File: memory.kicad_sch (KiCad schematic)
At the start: 43 parts, among them U1001 AM6231ASGGGAALW, U5001 K4AAG165WA-BCWE

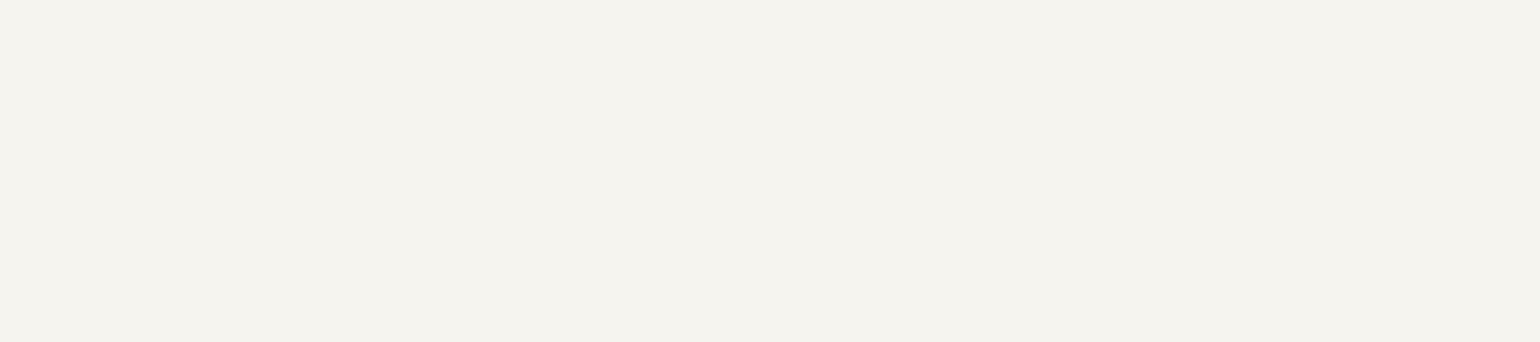
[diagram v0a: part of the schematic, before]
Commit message: Cleaned up schematic
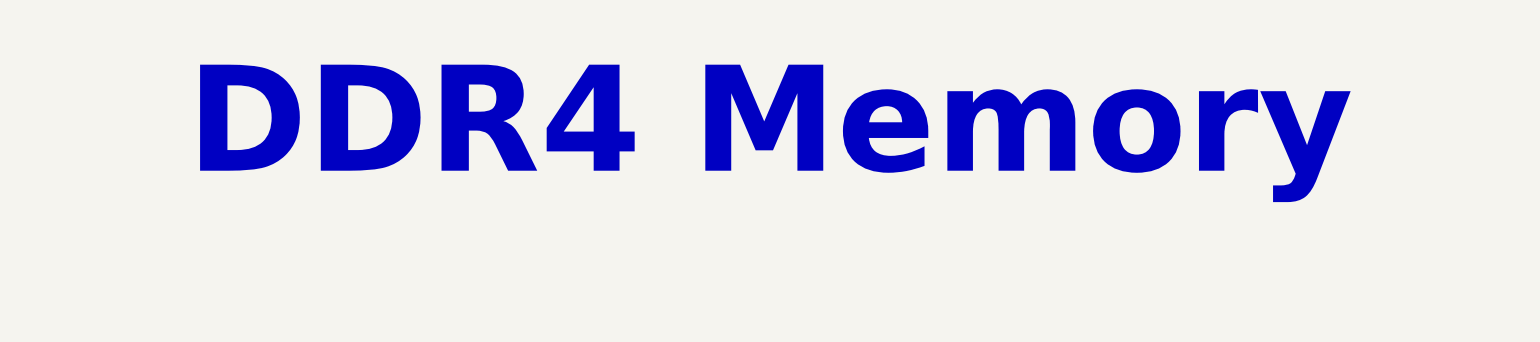
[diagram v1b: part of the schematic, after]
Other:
- note added: "DDR4 Memory"
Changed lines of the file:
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@@
+		)
+	)
+	(text "DDR4 Memory"
+		(exclude_from_sim no)
+		(at 187.452 47.498 0)
+		(effects
+			(font
+				(size 17.78 17.78)
+				(thickness 3.556)
+				(bold yes)
+			)
 		)
 	)

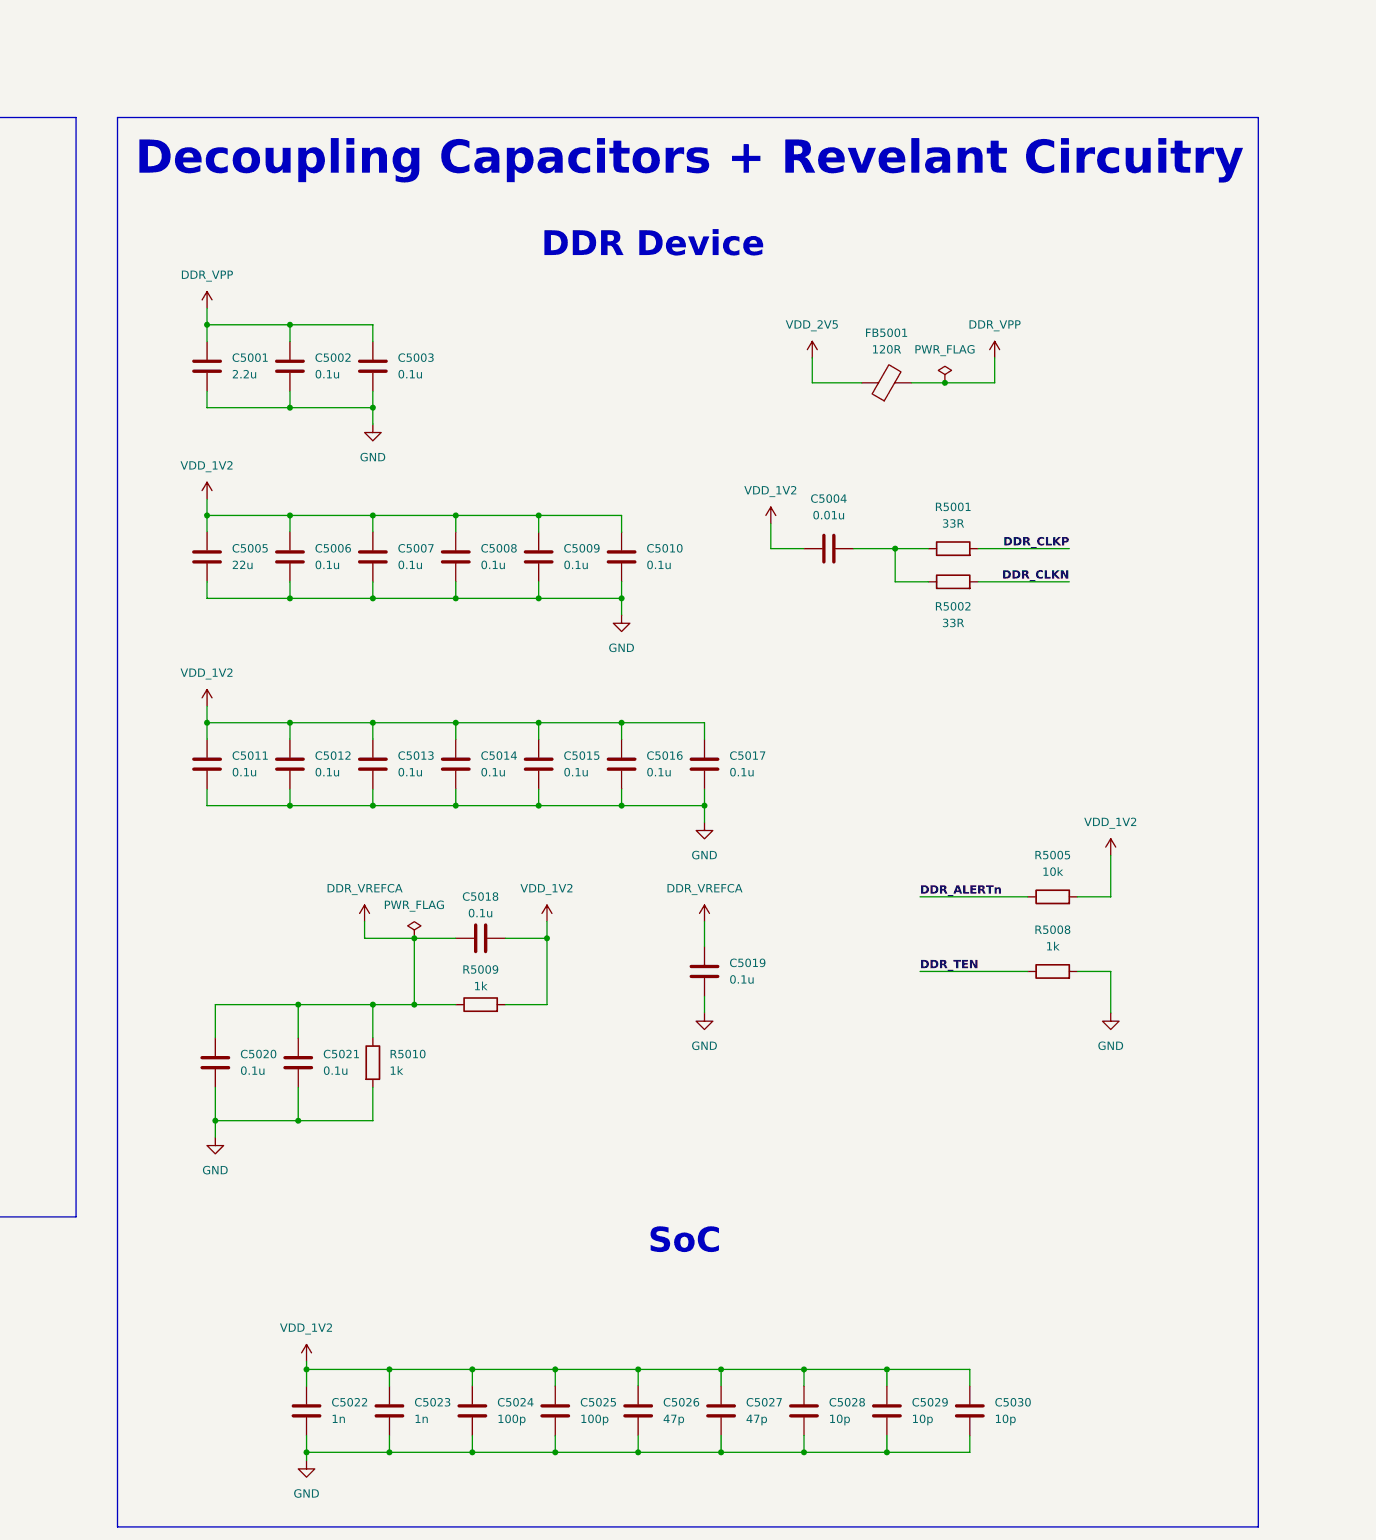
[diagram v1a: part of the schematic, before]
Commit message: Changed DDR4 decoupling capacitors and placed them
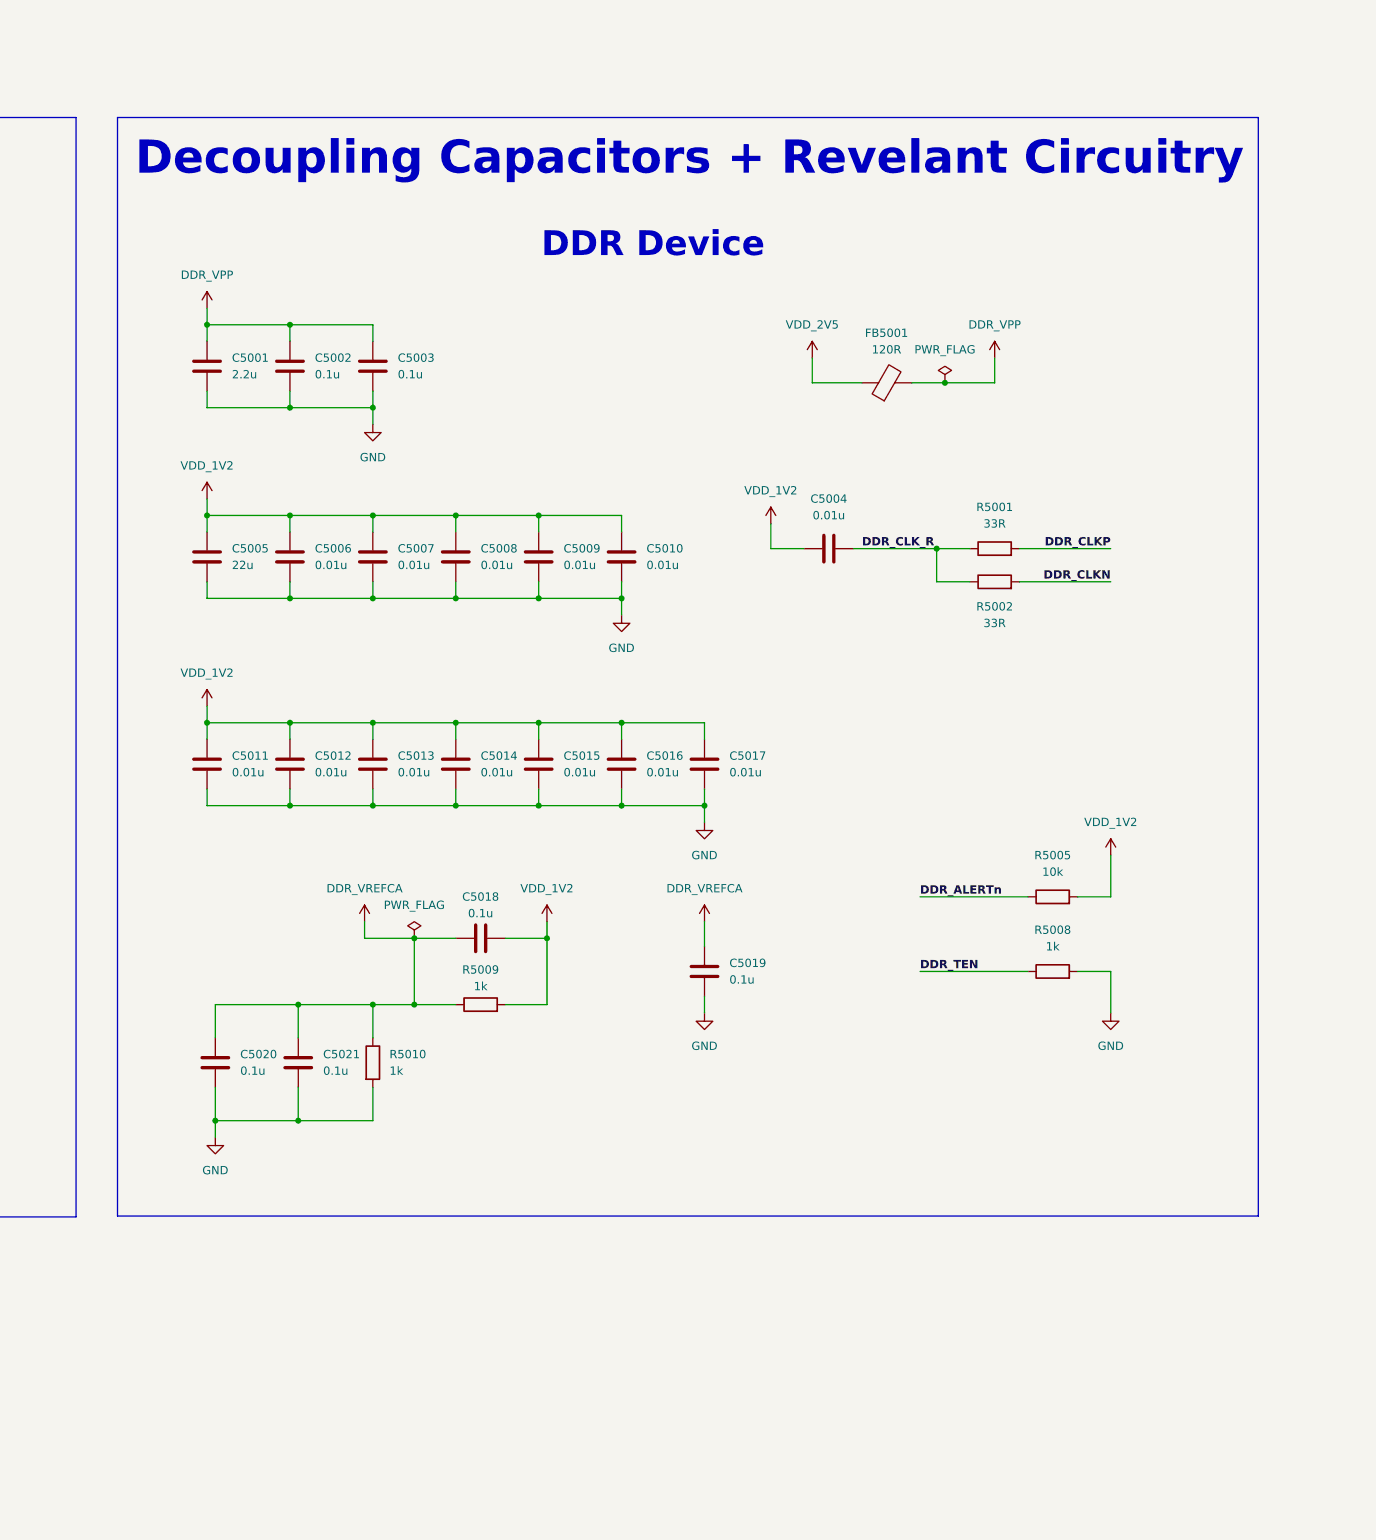
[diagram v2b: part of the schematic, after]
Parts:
- removed C5022, C5023: 1n, Capacitor_SMD:C_0201_0603Metric, symbol Device:C
- removed C5024, C5025: 100p, Capacitor_SMD:C_0201_0603Metric, symbol Device:C
- removed C5026, C5027: 47p, Capacitor_SMD:C_0201_0603Metric, symbol Device:C
- removed C5028, C5029, C5030: 10p, Capacitor_SMD:C_0201_0603Metric, symbol Device:C
- C5006, C5007, C5008, C5009, C5010, C5011, C5012, C5013, C5014, C5015, C5016, C5017: value 0.1u -> 0.01u
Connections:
- net DDR_CLK_R: now reaches C5004.2, R5001.1, R5002.1
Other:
- note removed: "SoC"
- moved on the sheet: R5001, R5002

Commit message: Placed all DDR4 external circuitry and added power puddles
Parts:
- R5005, R5008, R5009, R5010: footprint Resistor_SMD:R_0402_1005Metric -> Resistor_SMD:R_0201_0603Metric
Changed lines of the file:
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@@
 			)
 		)
-		(property "Footprint" "Resistor_SMD:R_0402_1005Metric"
+		(property "Footprint" "Resistor_SMD:R_0201_0603Metric"
 			(at 546.1 218.948 90)
 			(effects
@@
 			)
 		)
-		(property "Footprint" "Resistor_SMD:R_0402_1005Metric"
+		(property "Footprint" "Resistor_SMD:R_0201_0603Metric"
 			(at 440.182 231.14 90)
 			(effects
@@
 			)
 		)
-		(property "Footprint" "Resistor_SMD:R_0402_1005Metric"
+		(property "Footprint" "Resistor_SMD:R_0201_0603Metric"
 			(at 458.47 224.028 90)
 			(effects
@@
 			)
 		)
-		(property "Footprint" "Resistor_SMD:R_0402_1005Metric"
+		(property "Footprint" "Resistor_SMD:R_0201_0603Metric"
 			(at 546.1 207.518 90)
 			(effects

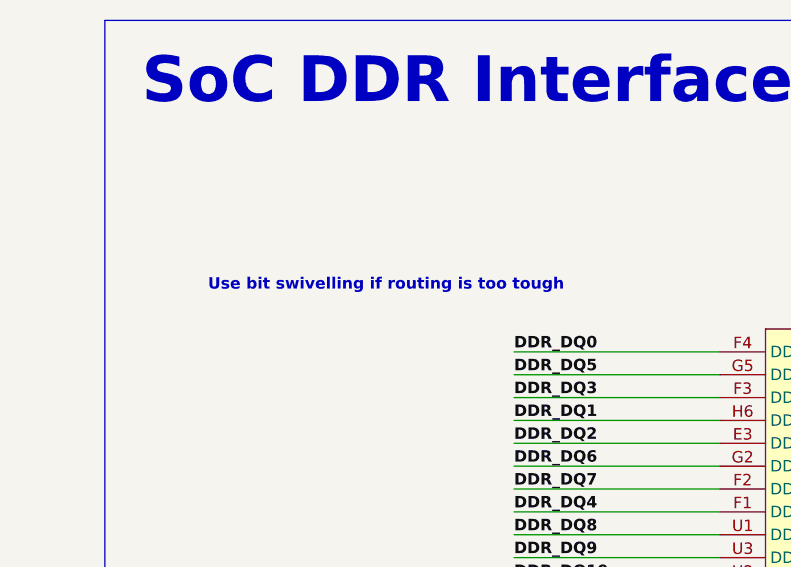
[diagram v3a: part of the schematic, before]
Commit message: Finished DDR4 length matching
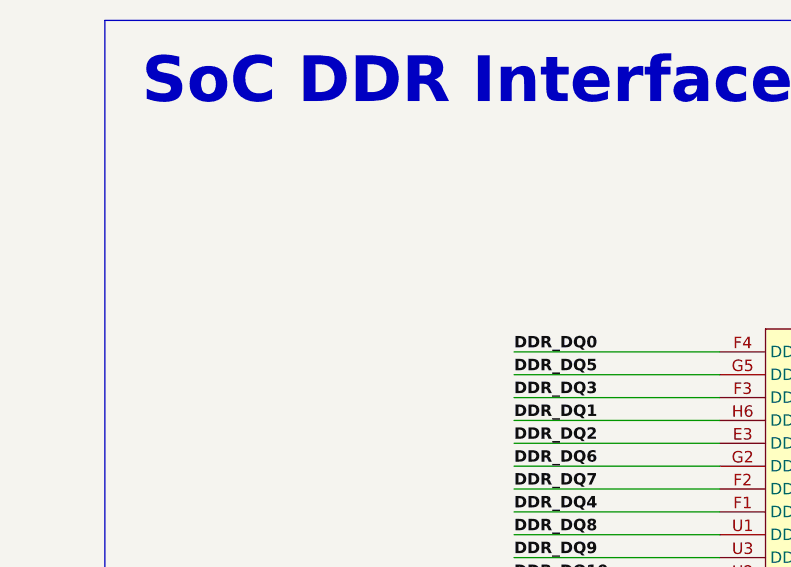
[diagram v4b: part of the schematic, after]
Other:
- note removed: "Use bit swivelling if routing is too tough"
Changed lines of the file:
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@@
-		)
-	)
-	(text "Use bit swivelling if routing is too tough"
-		(exclude_from_sim no)
-		(at 54.356 115.824 0)
-		(effects
-			(font
-				(size 1.27 1.27)
-				(thickness 0.254)
-				(bold yes)
-			)
 		)
 	)

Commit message: Added new radio schematic
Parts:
- renumbered C5001 to C4001, C5002 to C4002, C5003 to C4003, C5004 to C4004, C5005 to C4005, C5006 to C4006, C5007 to C4007, C5008 to C4008, C5009 to C4009, C5010 to C4010, C5011 to C4011, C5012 to C4012, C5013 to C4013, C5014 to C4014, C5015 to C4015, C5016 to C4016, C5017 to C4017, C5018 to C4018, C5019 to C4019, C5020 to C4020, C5021 to C4021, FB5001 to FB4001, R5001 to R4001, R5002 to R4002, R5003 to R4003, R5004 to R4004, R5005 to R4005, R5006 to R4006, R5007 to R4007, R5008 to R4008, R5009 to R4009, R5010 to R4010, U1001 to U1002, U5001 to U4001

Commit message: Small clean up
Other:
- moved on the sheet: C4001, C4002, C4003, C4004, C4005, C4006, C4007, C4008, C4009, C4010, C4011, C4012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

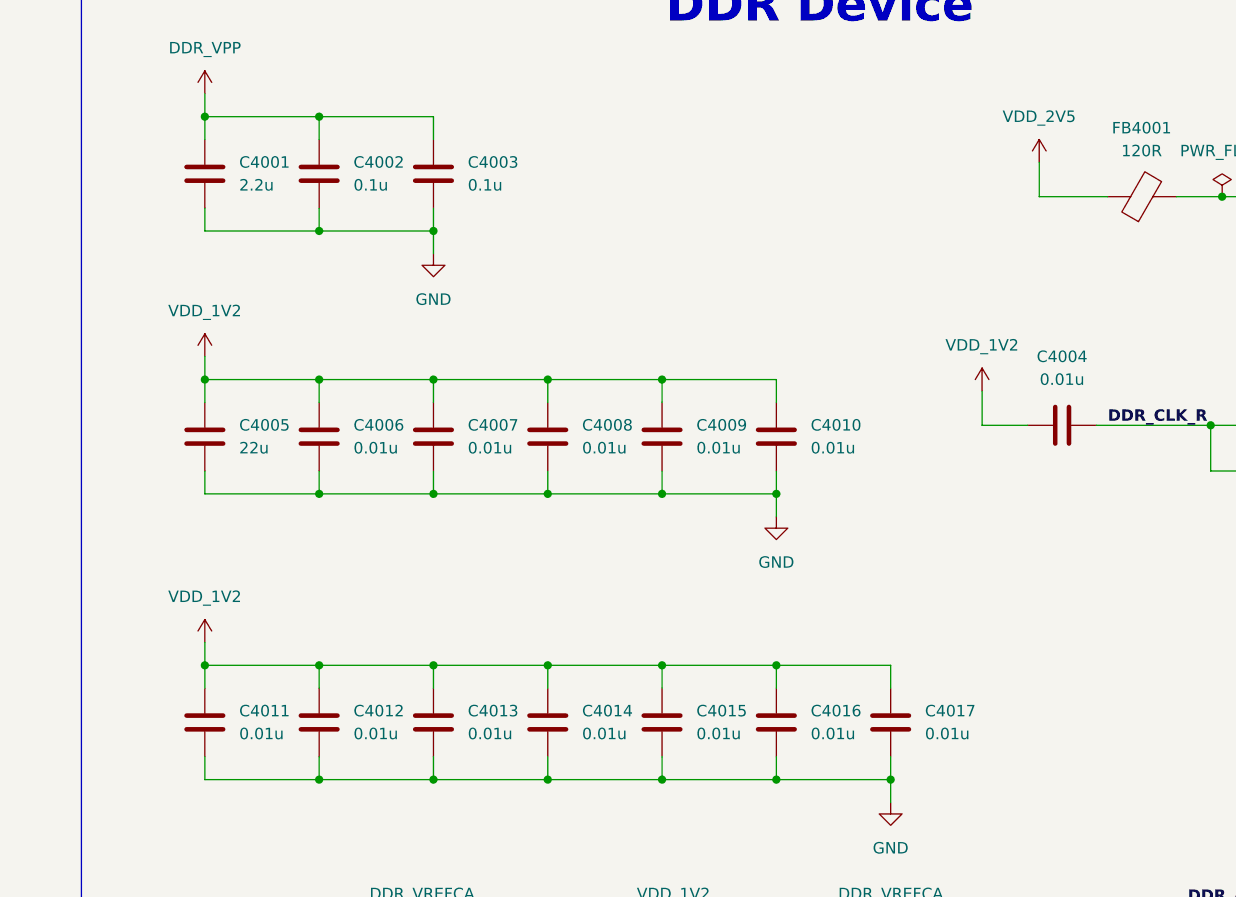
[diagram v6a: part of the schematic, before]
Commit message: Added JLCPCB part numbers for some caps
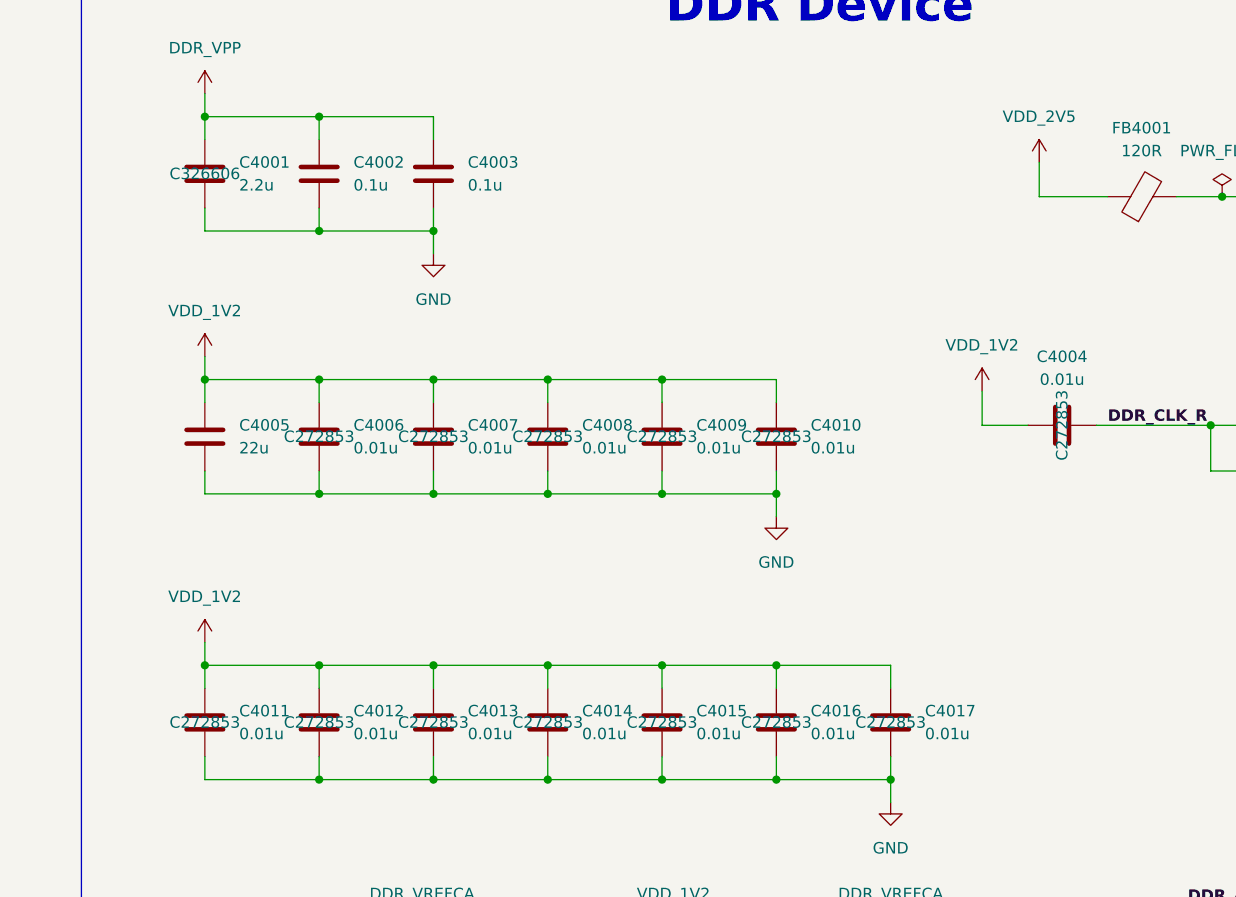
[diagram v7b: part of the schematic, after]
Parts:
- C4001: JLCPCB Part# (none) -> C326606
- C4004, C4006, C4007, C4008, C4009, C4010, C4011, C4012, C4013, C4014, C4015, C4016, C4017: JLCPCB Part# (none) -> C272853
